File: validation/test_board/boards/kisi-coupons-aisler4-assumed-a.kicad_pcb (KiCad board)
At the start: 4 copper layers, 35 x 144 mm, 22 parts, among them J1 292-04A-14, J10 292-04A-14, J11 292-04A-14, J12 292-04A-14, J13 292-04A-14, J14 292-04A-14, J15 292-04A-14, J16 292-04A-14, J17 292-04A-14, J18 292-04A-14, J19 292-04A-14, J2 292-04A-14, J20 292-04A-14, J21 292-04A-14, J22 292-04A-14, J3 292-04A-14, J4 292-04A-14, J5 292-04A-14, J6 292-04A-14, J7 292-04A-14, J8 292-04A-14, J9 292-04A-14

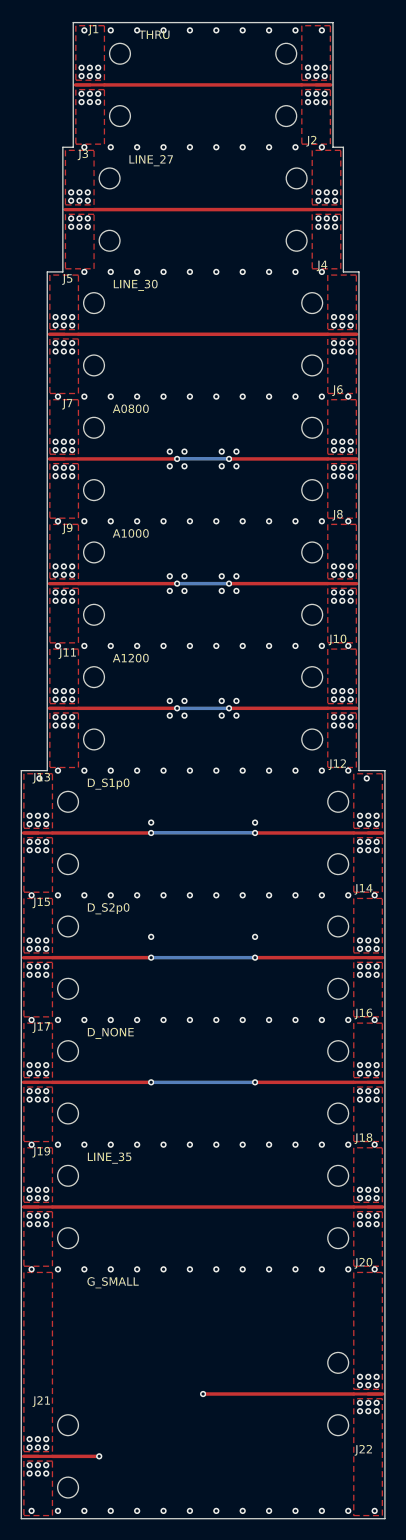
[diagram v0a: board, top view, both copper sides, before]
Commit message: Measurement coupons v3: Samtec 2.92 mm edge launch, 40 GHz plan
- Connector: Samtec 292-J-P-EP-ST-EL-01 (2.92 mm to 40 GHz, compression
  mount, PCB 1.02-2.54 mm; maintainer's decision 2026-10-30 on the RF
  group's advice) replaces the SMA Southwest 292-04A-14. Data, sources,
  the meaning of every footprint dimension of Samtec's drawing and the
  benchmark of Samtec's RF report (2023-06-01) in connectors.json.
- Footprint generated by make_coupons.py from parameters (Samtec's
  files are not committed: their terms forbid redistributing the
  models): geometry from drawing 292-J-P-EP-ST-EL-01-X-MKT rev C,
  plated screw holes 2.79 mm from the edge, +-2.92 mm, ground pads on
  top and bottom copper, signal tip 0.23 mm; marked DRAFT. The
  generator checks that no other net lies under the pads.
- Launch parametric (tip, taper, pad, coplanar section, ground cut,
  fence); default our 50 ohm coplanar launch inside the Samtec pads.
  --launch-cases writes kisi-fdtd cases; first runs (board side only)
  in fdtd_ref/launch_jlc4_7628: -18.9 dB worst to 40 GHz with the
  launch width to the edge, Samtec's 0.52 mm pad -14.6 dB.
- 40 GHz plan: stub notches of 6-layer VLV_L3 and 8-layer VLV_L6 now in
  the band, row via walls 2.54 -> 1.27 mm, measurement plan and ordering
  checklist to 40 GHz with 2.92 mm calibration and tools.
- Boards, manifests and 3D cases regenerated (widths unchanged); DRC
  with KiCad 7 on converted copies: no errors; kisi check rerun with
  kisi 0.3.1 (three v2 findings resolved in kisi since).

Co-Authored-By: Claude Opus 5.5 <noreply@anthropic.com>
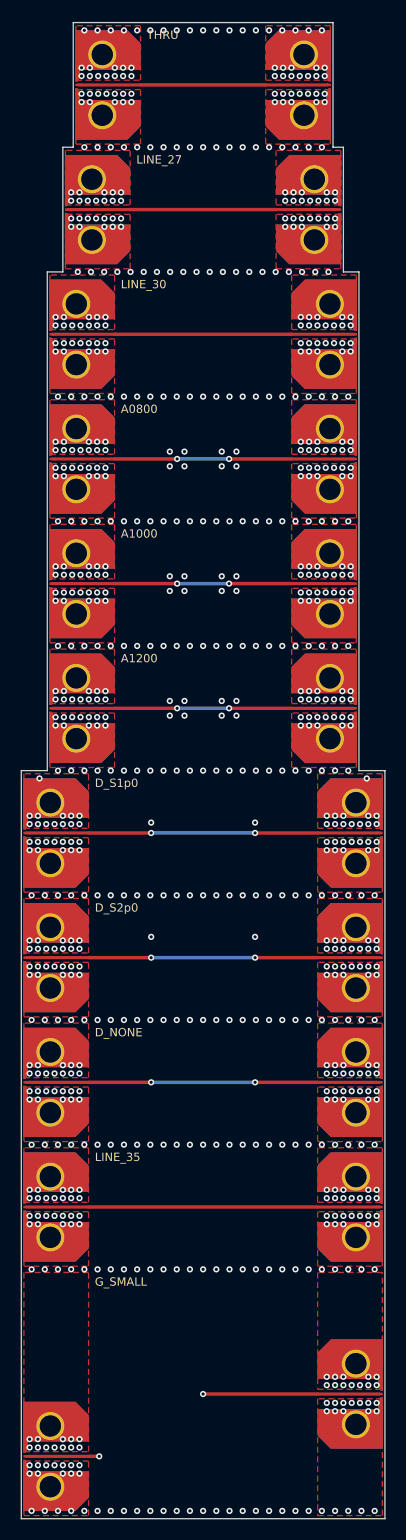
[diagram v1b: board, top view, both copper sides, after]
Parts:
- removed the J12 at (62.5, 96.0)
- added J17: 292-J-P-EP-ST-EL-01, kisi_coupons:Samtec_292-J-P-EP-ST-EL-01_EdgeLaunch, F.Cu at (30.0, 132.0)
- J1, J10, J11, J13, J14, J15, J16, J18, J19, J2, J20, J21, J22, J3, J4, J5, J6, J7, J8, J9: value 292-04A-14 -> 292-J-P-EP-ST-EL-01; footprint kisi_coupons:SWM_292-04A-14_EndLaunch_PLACEHOLDER -> kisi_coupons:Samtec_292-J-P-EP-ST-EL-01_EdgeLaunch
- J12: renamed from J17; value 292-04A-14 -> 292-J-P-EP-ST-EL-01; footprint kisi_coupons:SWM_292-04A-14_EndLaunch_PLACEHOLDER -> kisi_coupons:Samtec_292-J-P-EP-ST-EL-01_EdgeLaunch
- moved J12 48.5 mm to (62.5, 96.0), turned to 180 degrees
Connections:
- J12 pad 1: SE_D_NONE -> SE_A1200
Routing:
- net CAV_G_SMALL: track 24.6 -> 23.4 mm
- net SE_THRU: track 24.6 -> 23.4 mm
- net SE_LINE_35: track 34.6 -> 33.4 mm
- net SE_LINE_30: track 29.6 -> 28.4 mm
- net SE_LINE_27: track 26.6 -> 25.4 mm
- net SE_D_S2p0: track 34.6 -> 33.4 mm
- net SE_D_S1p0: track 34.6 -> 33.4 mm
- net SE_D_NONE: track 34.6 -> 33.4 mm
- net SE_A1200: track 29.6 -> 28.4 mm
- net SE_A1000: track 29.6 -> 28.4 mm
- net SE_A0800: track 29.6 -> 28.4 mm
- net GND: vias 442 -> 843
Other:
- board text added: "2026-10-30"
- board text added: "Connector footprint generated from Samtec's drawing (DRAFT, connectors.json); launch not yet optimised."
- board text added: "Copper comes to 0.2 mm from the left/right edges at the 2.92 mm edge launches (Samtec 292-J-P-EP-ST-EL-01, plated screw holes)."
- board text added: "assumed stackup v3"
- board text added: "kisi-coupons-aisler4-assumed-a: kisi measurement coupons v3 (2026-10-30)"
- board text removed: "Connector footprint is a PLACEHOLDER (connectors.json) until the vendor drawing is supplied."
- board text removed: "Copper comes to 0.2 mm from the left/right edges at the SMA end launches (Southwest Microwave 292-04A-14)."
- board text removed: "assumed stackup v2 2026-10-22"
- board text removed: "kisi-coupons-aisler4-assumed-a: kisi measurement coupons v2 (2026-10-22)"

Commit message: Launch optimisation step 1: launch width to the edge, fence 0.55 mm
- kisi-fdtd launch cases on the 7628 stack, board side (the connector's
  coax not modelled): our 50 ohm coplanar launch run to the edge with a
  0.55 mm fence from 0.5 mm gives |S11| -21.0 dB at worst to 40 GHz;
  the 0.8 mm draft fence left |S21| dips at 25-38 GHz (-18.9 dB),
  Samtec's 0.23 mm tip -15.7 dB (-16.8 dB with the pin modelled), its
  0.52 mm pad -14.6 dB. These become the defaults in connectors.json;
  the variants are named after what they change, results in
  fdtd_ref/launch_jlc4_7628. The jaw case is still not valid.
- Boards regenerated with the new launch (DRC with KiCad 7: no errors),
  kisi check rerun.
- The connector is in stock at DigiKey (maintainer): the boards set the
  timeline.

Co-Authored-By: Claude Opus 5.5 <noreply@anthropic.com>
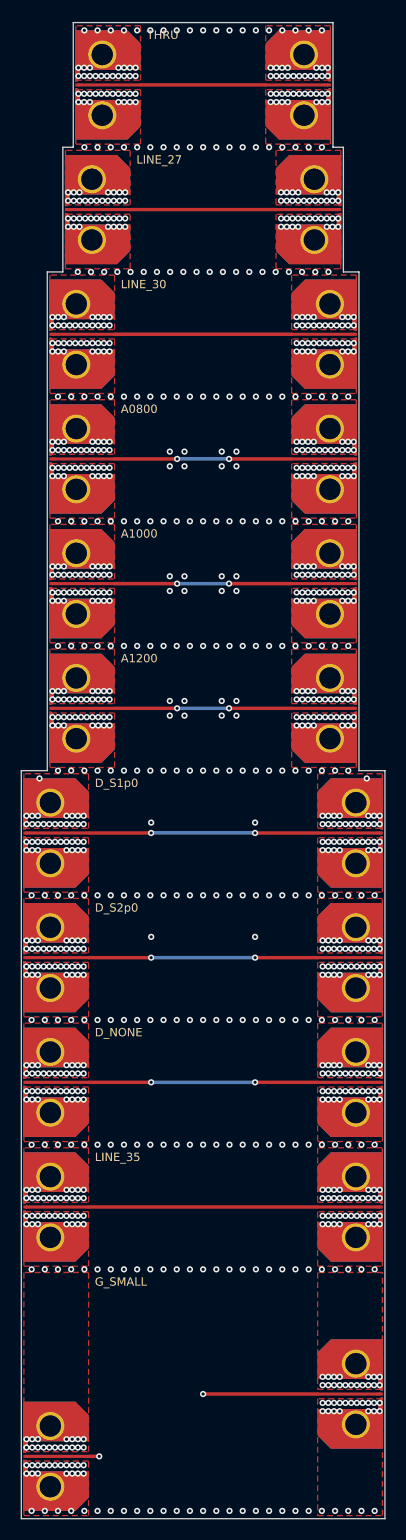
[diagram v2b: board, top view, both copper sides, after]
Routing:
- net GND: vias 843 -> 1107
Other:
- board text added: "Connector footprint generated from Samtec's drawing (DRAFT, connectors.json); launch from a first kisi-fdtd optimisation step."
- board text removed: "Connector footprint generated from Samtec's drawing (DRAFT, connectors.json); launch not yet optimised."

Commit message: Coupon boards: own zone priorities, project-local footprint library
- KiCad 8/9 DRC reported overlapping zones of equal priority (the GND
  pour rectangles on L1 meet at 4-port launch pairs and along the CPWG
  coupons: 78 pairs on 26 boards). Every zone now has its own priority
  (planes 0, pours 1, 2, ..., islands and patches above); an outline
  check finds no equal-priority overlap left.
- The footprints the boards use are written as a project-local library
  (boards/kisi_coupons.pretty + fp-lib-table with ${KIPRJMOD}): the
  Samtec launch per launch width, the capacitor land patterns, the IC
  pin fields; per-instance Port/Status fields dropped, so board and
  library match. DRC (KiCad 7 on converted copies, with the library):
  no library warnings, no errors; the first-order boards are clean.
- Boards regenerated, kisi check unchanged.

Co-Authored-By: Claude Opus 5.5 <noreply@anthropic.com>
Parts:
- removed the J17 at (30.0, 132.0)
- removed the J9 at (32.5, 84.0)
- added J15: 292-J-P-EP-ST-EL-01, kisi_coupons:Samtec_292-J-P-EP-ST-EL-01_EdgeLaunch_W0.305, F.Cu at (30.0, 120.0)
- added J8: 292-J-P-EP-ST-EL-01, kisi_coupons:Samtec_292-J-P-EP-ST-EL-01_EdgeLaunch_W0.305, F.Cu at (62.5, 72.0)
- J1, J10, J11, J12, J13, J14, J16, J18, J19, J2, J20, J21, J22, J3, J4, J5, J6, J7: footprint kisi_coupons:Samtec_292-J-P-EP-ST-EL-01_EdgeLaunch -> kisi_coupons:Samtec_292-J-P-EP-ST-EL-01_EdgeLaunch_W0.305
- J17: renamed from J15; footprint kisi_coupons:Samtec_292-J-P-EP-ST-EL-01_EdgeLaunch -> kisi_coupons:Samtec_292-J-P-EP-ST-EL-01_EdgeLaunch_W0.305
- J9: renamed from J8; footprint kisi_coupons:Samtec_292-J-P-EP-ST-EL-01_EdgeLaunch -> kisi_coupons:Samtec_292-J-P-EP-ST-EL-01_EdgeLaunch_W0.305
- moved J9 32.3 mm to (32.5, 84.0), turned to 0 degrees
- moved J17 12.0 mm to (30.0, 132.0)
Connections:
- J17 pad 1: SE_D_S2p0 -> SE_D_NONE
- J9 pad 1: SE_A0800 -> SE_A1000
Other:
- board text added: "2026-10-31"
- board text added: "kisi-coupons-aisler4-assumed-a: kisi measurement coupons v3 (2026-10-31)"
- board text removed: "2026-10-30"
- board text removed: "kisi-coupons-aisler4-assumed-a: kisi measurement coupons v3 (2026-10-30)"
